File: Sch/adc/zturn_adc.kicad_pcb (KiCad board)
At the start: 4 copper layers, 86 x 75.8 mm, 117 parts, among them CN1 SMA, CN2 SMA, CN3 AudioJack, J1 JP4, J2 Header5, J3 JP2, J4 JP2, J5 JP2, J6 JP2, P1 CONN_02X40, U1 LTC2292, U2 BGA2818, U3 TLV702, U4 BGA2818, U5 CDCLVC1102, U6 NAU8822LYG, U7 TLV702, X1 SIT5001

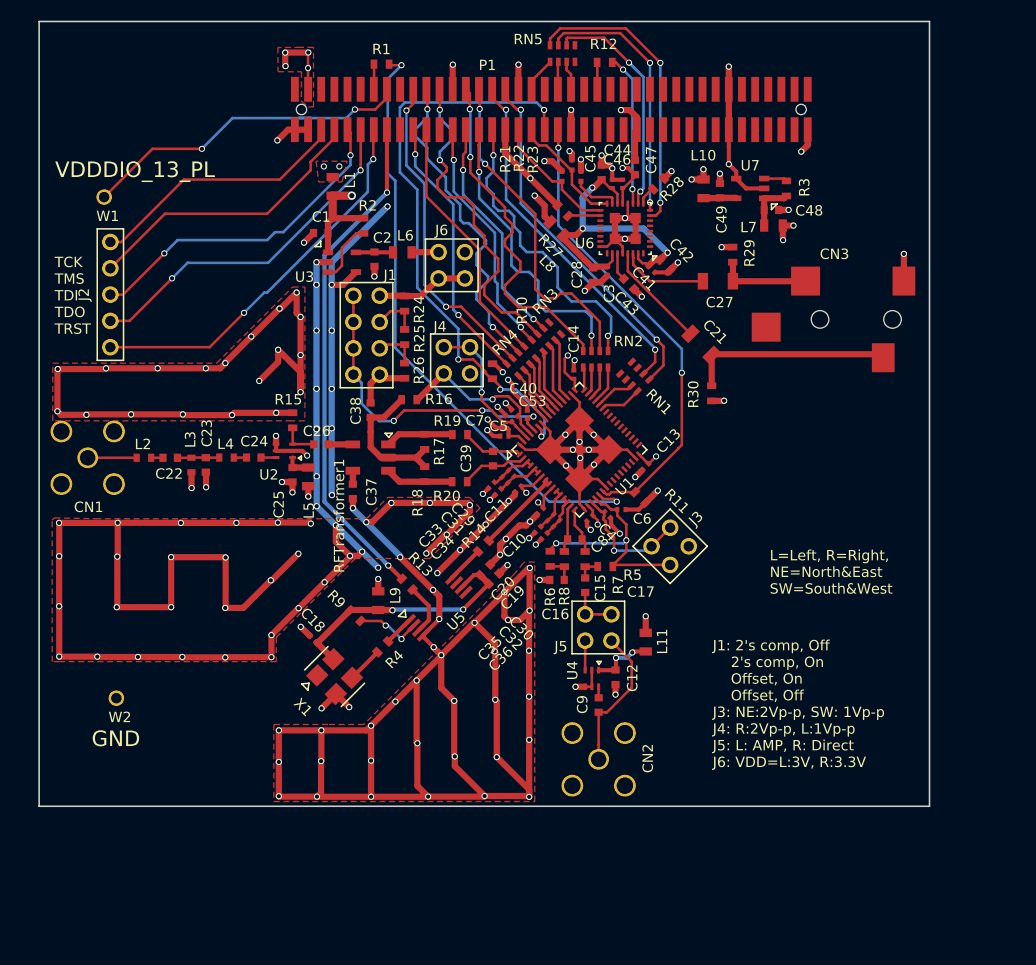
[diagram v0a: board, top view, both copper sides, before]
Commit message: Changed zone clearance to 0.3mm. Add silkscreen of the revision.
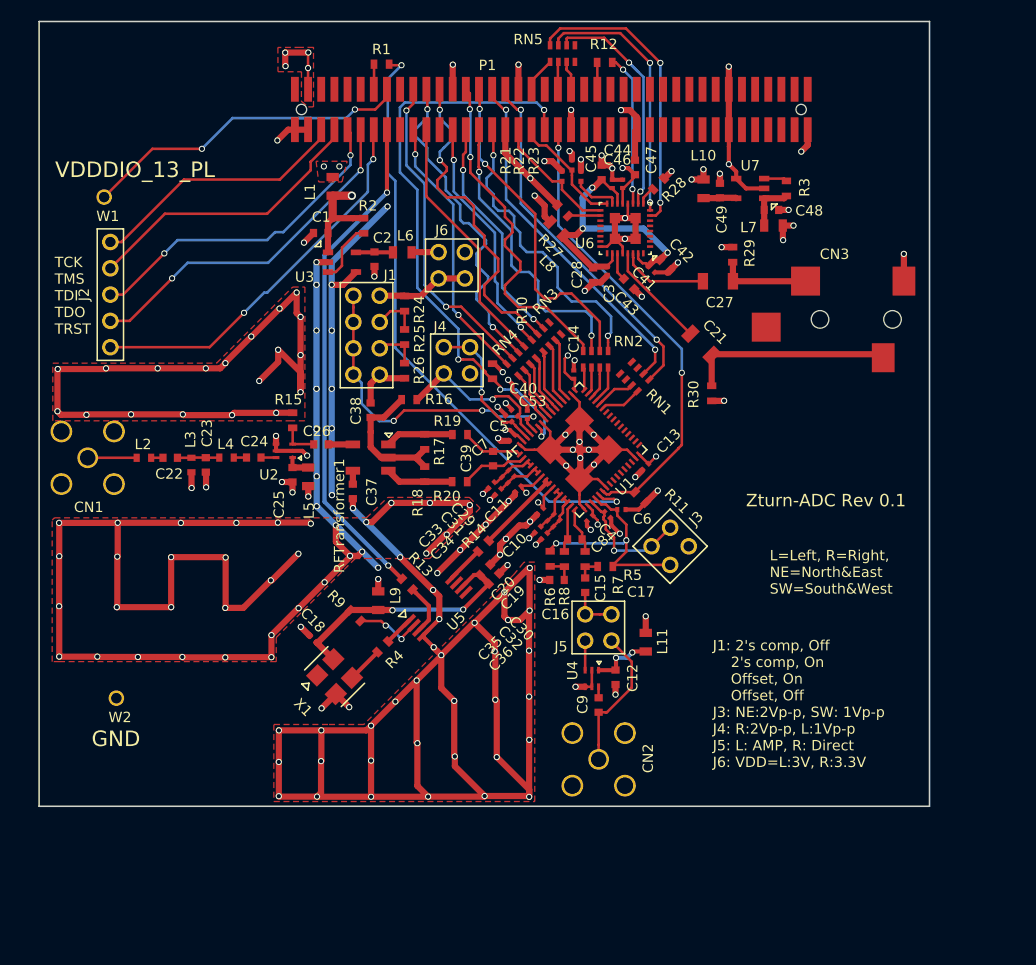
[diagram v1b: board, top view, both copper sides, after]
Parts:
- moved C7 0.75 mm to (137.2, 95.2), turned to 225 degrees
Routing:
- net VDD3: track 22.3 -> 19.9 mm
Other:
- board text added: "Zturn-ADC Rev 0.1"

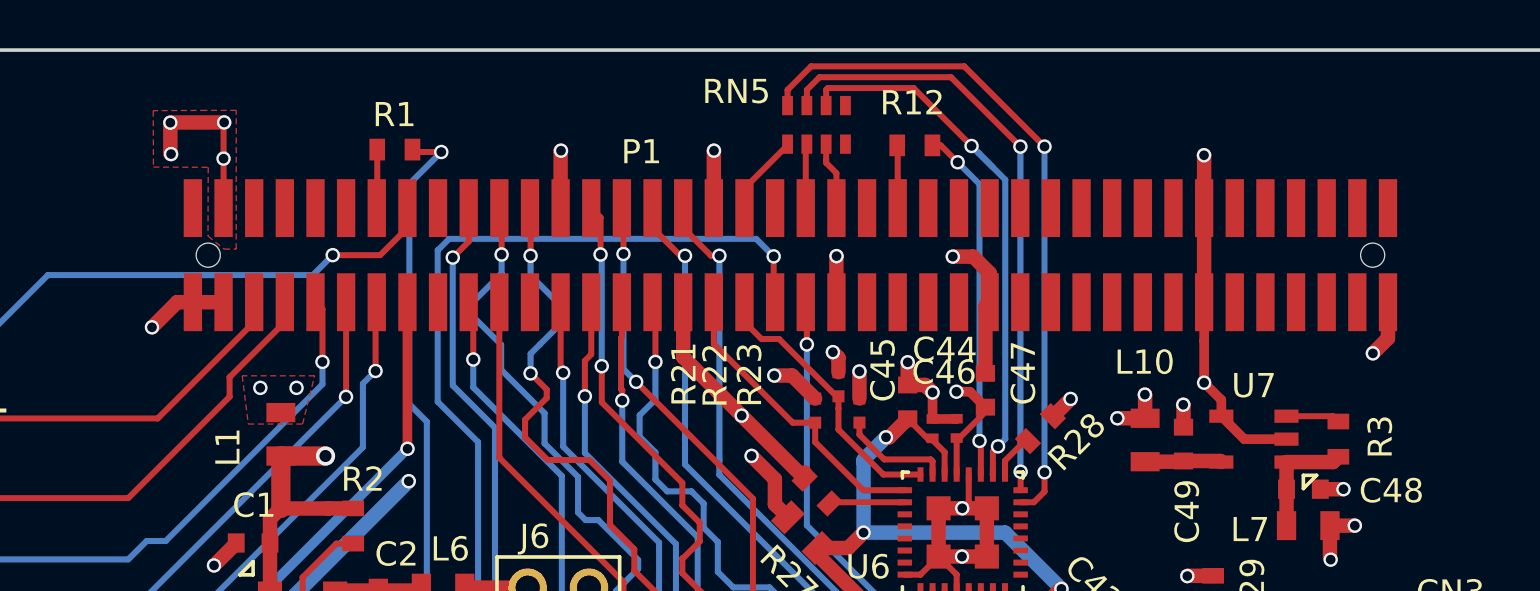
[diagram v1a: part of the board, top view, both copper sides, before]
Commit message: Fixed GND short of pin 80
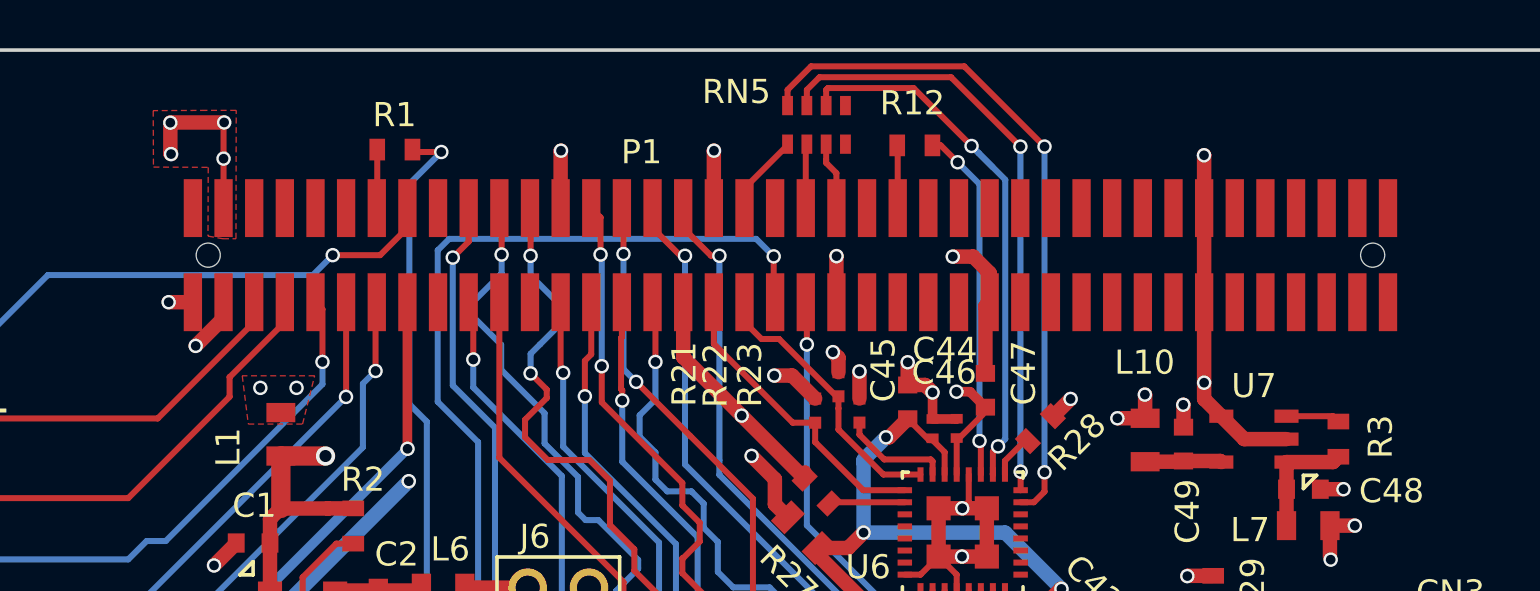
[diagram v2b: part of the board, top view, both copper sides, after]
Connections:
- P1 pad 80: GND -> Net-(P1-Pad80)
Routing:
- net GND: track 626.2 -> 624.4 mm
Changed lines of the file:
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@@
 (kicad_pcb (version 4) (host pcbnew 4.0.5)
   (general
-    (links 301)
+    (links 300)
     (no_connects 1)
     (area 91.424999 54.924999 177.575001 130.875001)
     (thickness 1.6)
     (drawings 12)
-    (tracks 1499)
+    (tracks 1497)
     (zones 0)
     (modules 117)
-    (nets 189)
+    (nets 190)
   )
   (page A4)
@@
   (net 187 "Net-(C12-Pad1)")
   (net 188 "Net-(C25-Pad2)")
+  (net 189 "Net-(P1-Pad80)")
   (net_class Default "これは標準のネット クラスです。"
     (clearance 0.2)
@@
     (add_net "Net-(P1-Pad78)")
     (add_net "Net-(P1-Pad79)")
+    (add_net "Net-(P1-Pad80)")
     (add_net "Net-(R2-Pad2)")
     (add_net "Net-(R23-Pad1)")
@@
       (net 106 "Net-(P1-Pad79)"))
     (pad 80 smd rect (at 24.765 1.95) (size 0.76 2.4) (layers F.Cu F.Paste F.Mask)
-      (net 2 GND))
+      (net 189 "Net-(P1-Pad80)"))
     (pad "" np_thru_hole circle (at 24.13 0) (size 1 1) (drill 1) (layers *.Cu *.Mask))
     (pad "" np_thru_hole circle (at -24.13 0) (size 1 1) (drill 1) (layers *.Cu *.Mask))
@@
   (segment (start 149.455065 96.833313) (end 150.360876 97.739124) (width 0.25) (layer F.Cu) (net 1))
   (segment (start 122.845 74) (end 122.85 73.995) (width 0.25) (layer F.Cu) (net 1))
+  (segment (start 117.475 65.45) (end 117.475 66.105) (width 0.6) (layer F.Cu) (net 2))
+  (segment (start 117.475 66.105) (end 116.32 67.26) (width 0.6) (layer F.Cu) (net 2))
+  (via (at 116.32 67.26) (size 0.6) (drill 0.4) (layers F.Cu B.Cu) (net 2))
+  (segment (start 116.205 65.45) (end 115.2 65.45) (width 0.6) (layer F.Cu) (net 2))
+  (via (at 115.2 65.45) (size 0.6) (drill 0.4) (layers F.Cu B.Cu) (net 2))
+  (segment (start 117.475 65.45) (end 117.475 66.155) (width 0.6) (layer F.Cu) (net 2))
+  (segment (start 158.82827 70.17494) (end 159.77827 71.12494) (width 0.6) (layer F.Cu) (net 2))
+  (segment (start 159.77827 71.12494) (end 161.52827 71.12494) (width 0.6) (layer F.Cu) (net 2))
+  (segment (start 158.115 68.78667) (end 158.115 69.46167) (width 0.6) (layer F.Cu) (net 2))
+  (segment (start 158.115 69.46167) (end 158.82827 70.17494) (width 0.6) (layer F.Cu) (net 2))
+  (segment (start 158.115 68.78667) (end 158.115 65.45) (width 0.6) (layer F.Cu) (net 2))
   (segment (start 136.887157 95.502843) (end 136.082843 95.502843) (width 0.6) (layer F.Cu) (net 2))
   (segment (start 136.082843 95.502843) (end 135.83 95.25) (width 0.6) (layer F.Cu) (net 2))
@@
   (segment (start 146.87 70.205) (end 146.86 70.215) (width 0.4) (layer F.Cu) (net 2))
   (via (at 158.115 68.78667) (size 0.6) (drill 0.4) (layers F.Cu B.Cu) (net 2))
-  (segment (start 158.82827 70.17494) (end 158.82827 69.49994) (width 0.4) (layer F.Cu) (net 2))
-  (segment (start 158.82827 69.49994) (end 158.115 68.78667) (width 0.4) (layer F.Cu) (net 2))
-  (segment (start 158.115 68.78667) (end 158.115 67.05) (width 0.4) (layer F.Cu) (net 2))
-  (segment (start 158.115 67.05) (end 158.115 65.45) (width 0.4) (layer F.Cu) (net 2))
   (segment (start 146.755876 103.025876) (end 146.755876 103.635876) (width 0.4) (layer F.Cu) (net 2))
   (segment (start 146.755876 103.635876) (end 147.59 104.47) (width 0.4) (layer F.Cu) (net 2))
@@
   (segment (start 175.025 77.455) (end 175.02 77.45) (width 0.6) (layer F.Cu) (net 2))
   (via (at 175.02 77.45) (size 0.6) (drill 0.4) (layers F.Cu B.Cu) (net 2))
-  (segment (start 165.735 65.45) (end 165.735 66.945) (width 0.6) (layer F.Cu) (net 2))
-  (segment (start 165.735 66.945) (end 165.11 67.57) (width 0.6) (layer F.Cu) (net 2))
-  (via (at 165.11 67.57) (size 0.6) (drill 0.4) (layers F.Cu B.Cu) (net 2))
   (segment (start 142.875 65.45) (end 142.875 63.545) (width 0.6) (layer F.Cu) (net 2))
   (segment (start 142.875 63.545) (end 142.88 63.54) (width 0.6) (layer F.Cu) (net 2))
@@
   (segment (start 131.445 59.185) (end 131.46 59.17) (width 0.6) (layer F.Cu) (net 2))
   (via (at 131.46 59.17) (size 0.6) (drill 0.4) (layers F.Cu B.Cu) (net 2))
-  (segment (start 116.205 65.45) (end 115.55 65.45) (width 0.6) (layer F.Cu) (net 2))
-  (segment (start 115.55 65.45) (end 114.51 66.49) (width 0.6) (layer F.Cu) (net 2))
-  (via (at 114.51 66.49) (size 0.6) (drill 0.4) (layers F.Cu B.Cu) (net 2))
-  (segment (start 117.475 65.45) (end 116.205 65.45) (width 0.6) (layer F.Cu) (net 2))
-  (segment (start 158.82827 70.17494) (end 159.77827 71.12494) (width 0.4) (layer F.Cu) (net 2))
-  (segment (start 159.77827 71.12494) (end 161.52827 71.12494) (width 0.4) (layer F.Cu) (net 2))
   (segment (start 158.115 61.55) (end 158.115 65.45) (width 0.6) (layer F.Cu) (net 2))
   (segment (start 136.525 67.725) (end 136.525 65.45) (width 0.6) (layer F.Cu) (net 2))
@@
       (pts
         (xy 116.75 57.5) (xy 114.56 57.51) (xy 114.57 59.85) (xy 116.84 59.86) (xy 116.83 62.71)
-        (xy 117.5 63.25) (xy 118 63.25) (xy 118 57.5)
+        (xy 117.45 62.82) (xy 117.99 62.82) (xy 118 57.5)
       )
     )

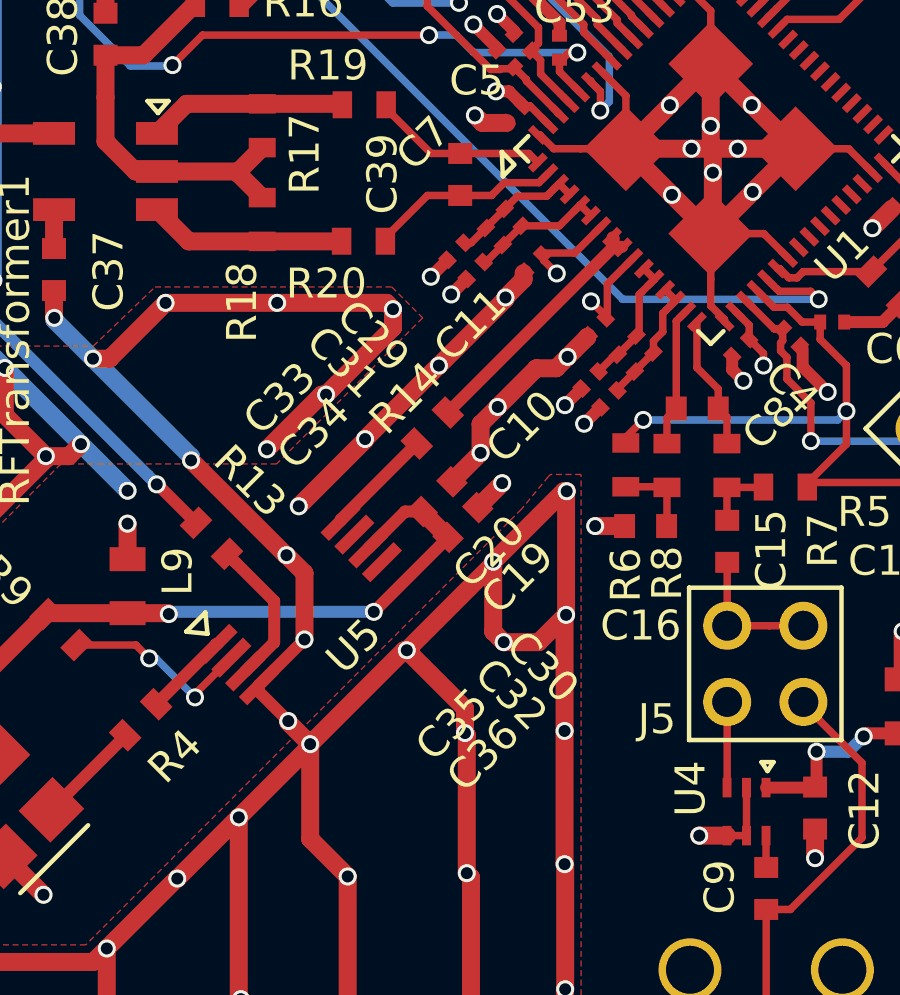
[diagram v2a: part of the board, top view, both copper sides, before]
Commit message: Moved reference caps close to ADC
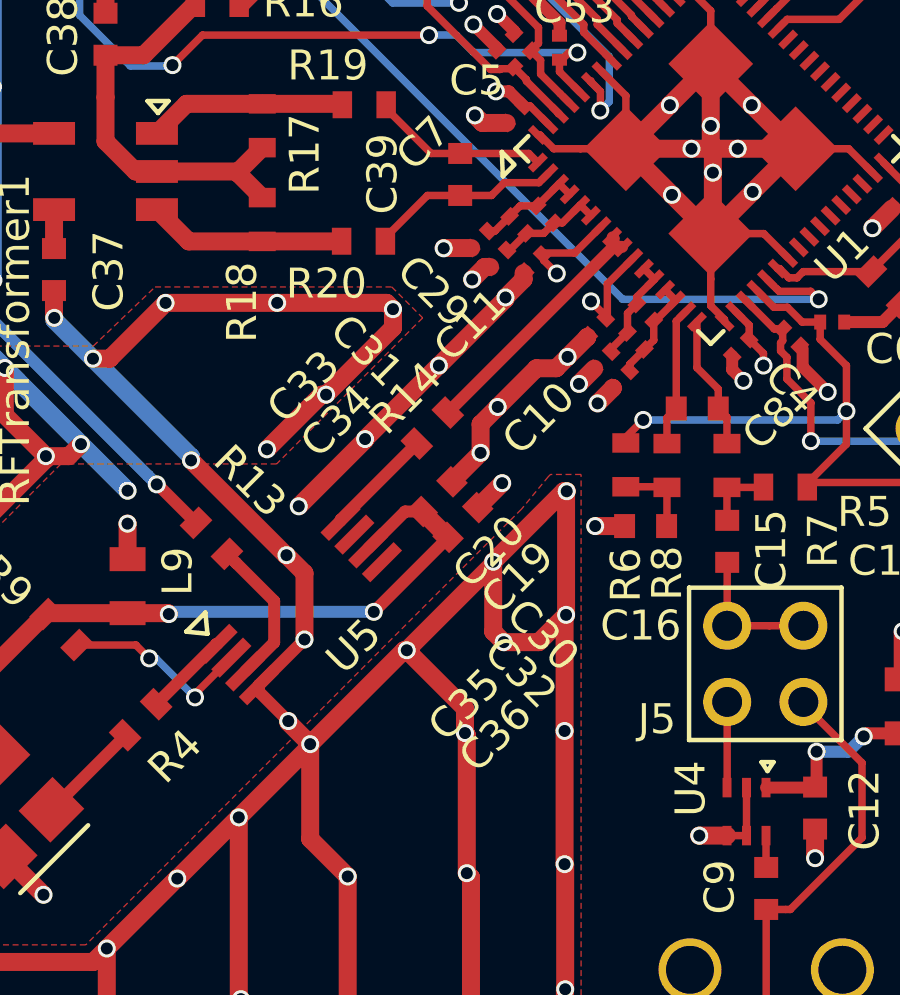
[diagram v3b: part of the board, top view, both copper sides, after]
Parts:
- moved C29 1.08 mm to (138.2, 98.5)
- moved C30 1.06 mm to (141.5, 101.8)
- moved C31 0.88 mm to (137.3, 98.9)
- moved C33 0.88 mm to (136.0, 99.4)
- moved C34 0.88 mm to (136.6, 100.0)
- moved C32 0.81 mm to (141.2, 102.8)
- moved C35 0.78 mm to (140.1, 103.4)
- moved C36 0.77 mm to (140.7, 104.0)
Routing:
- net Net-(C29-Pad1): track 4.50 -> 3.52 mm
- net Net-(C29-Pad2): track 4.51 -> 3.56 mm
- net Net-(C30-Pad2): track 4.30 -> 3.51 mm
- net Net-(C30-Pad1): track 4.22 -> 3.51 mm
